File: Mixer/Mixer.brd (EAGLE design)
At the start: 94 x 59 mm, 49 parts, among them IC1 LM741P, IC2 LM741P, T1 2N3904

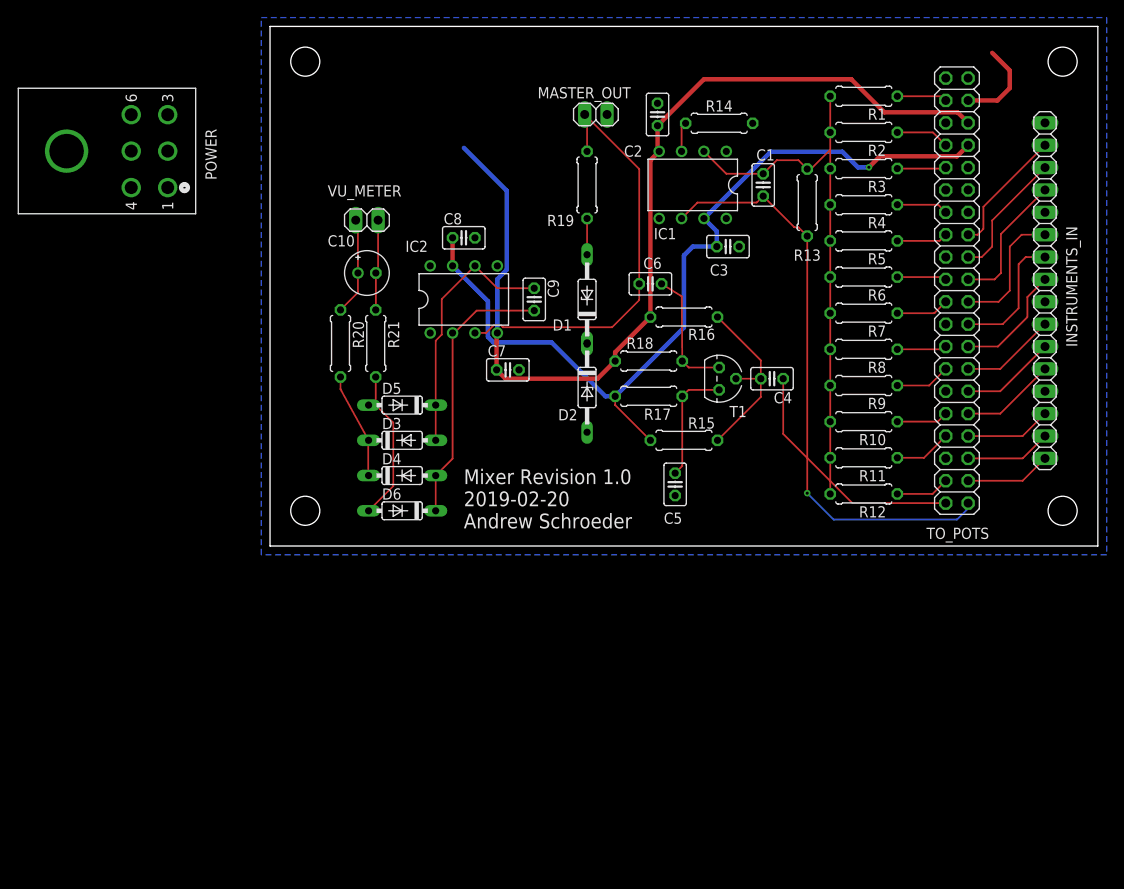
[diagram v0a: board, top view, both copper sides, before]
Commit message: Completed Mixer Board Layout
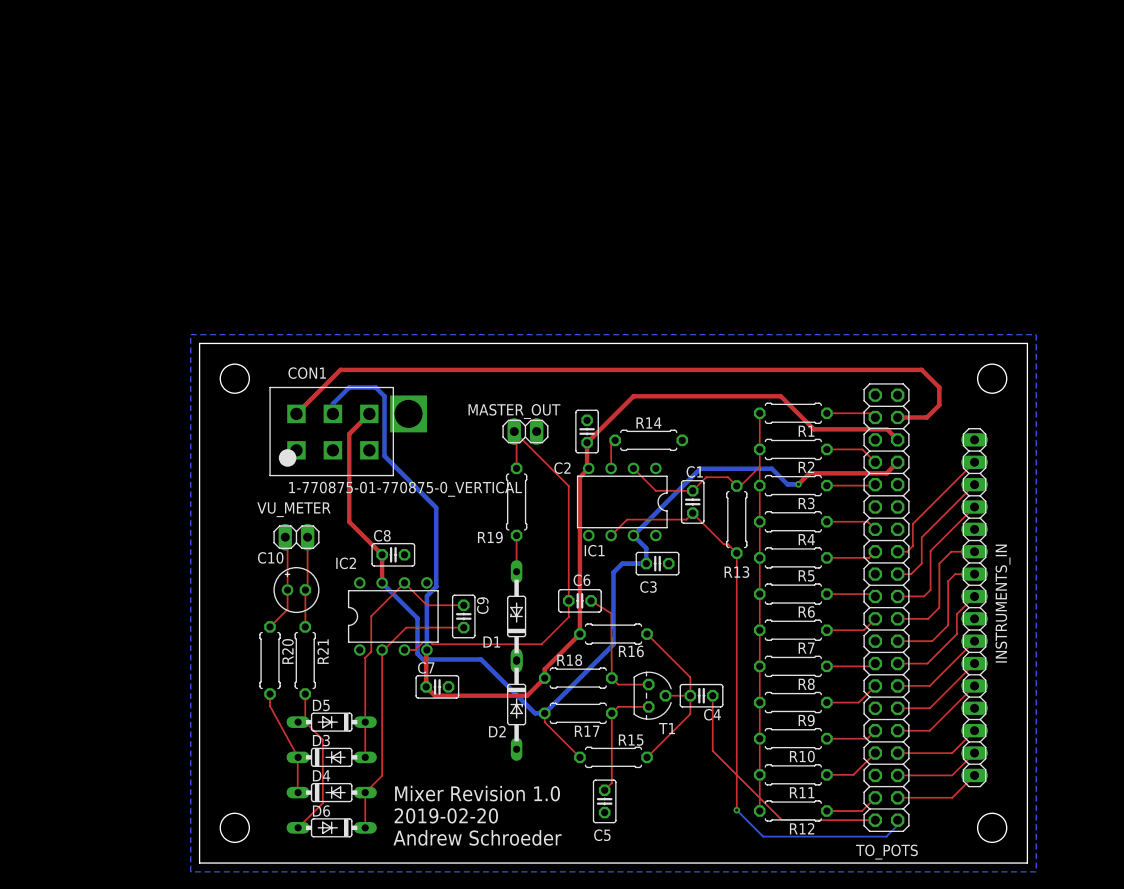
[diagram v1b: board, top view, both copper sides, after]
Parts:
- removed POWER: 1-770875-0, Capstone:CON6_2X3_P163_RAMNL
- added CON1: 1-770875-01-770875-0_VERTICAL, Capstone:1-770875-0
- added U$5: (no value), frames:A4L-LOC
- moved R1 36.9 mm to (67.4, 51.1)
- moved R6 36.9 mm to (67.4, 30.5)
- moved C1 36.9 mm to (56.0, 41.0)
- moved C10 36.9 mm to (11.0, 31.0)
- moved C2 36.9 mm to (44.0, 49.0)
- moved C3 36.9 mm to (52.0, 34.0)
- moved C4 36.9 mm to (57.0, 19.0)
- moved C5 36.9 mm to (46.0, 7.00)
- moved C6 36.9 mm to (43.2, 29.8)
- moved C7 36.9 mm to (27.0, 20.0)
- moved C8 36.9 mm to (22.0, 35.0)
- moved C9 36.9 mm to (30.0, 28.0)
- moved D1 36.9 mm to (36.0, 28.0)
- moved D2 36.9 mm to (36.0, 18.0)
- moved D3 36.9 mm to (15.0, 12.0)
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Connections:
- net +12V: now also CON1.4; no longer POWER.4
- net +5V: now also CON1.6; no longer POWER.6
- net -12V: now also CON1.5; no longer POWER.5
- net GND: now also CON1.1, CON1.2, CON1.3; no longer POWER.1, POWER.2, POWER.3
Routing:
- net +5V: track 10.1 -> 83.2 mm
- net +12V: track 98.9 -> 117.4 mm
- net -12V: track 111.3 -> 127.2 mm
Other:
- board text added: "Andrew Schroeder"
- board text added: "Revision 1.0"
